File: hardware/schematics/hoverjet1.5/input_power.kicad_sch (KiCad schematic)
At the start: 12 parts, among them J1 Barrel_Jack, J2 Molex MiniFit 3.0

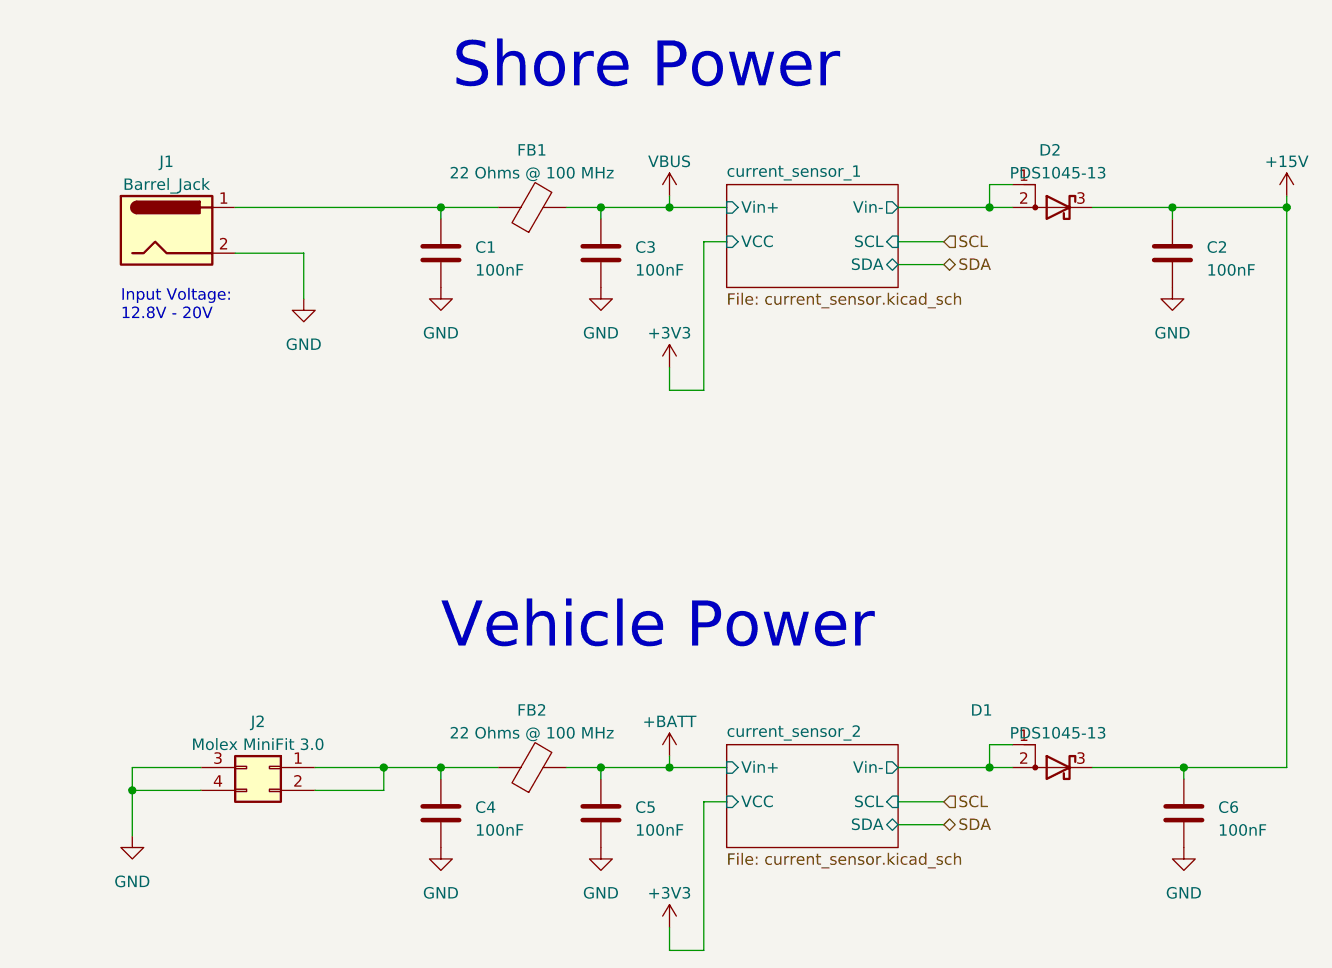
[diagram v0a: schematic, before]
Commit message: Added LM5050 ideal diode controller
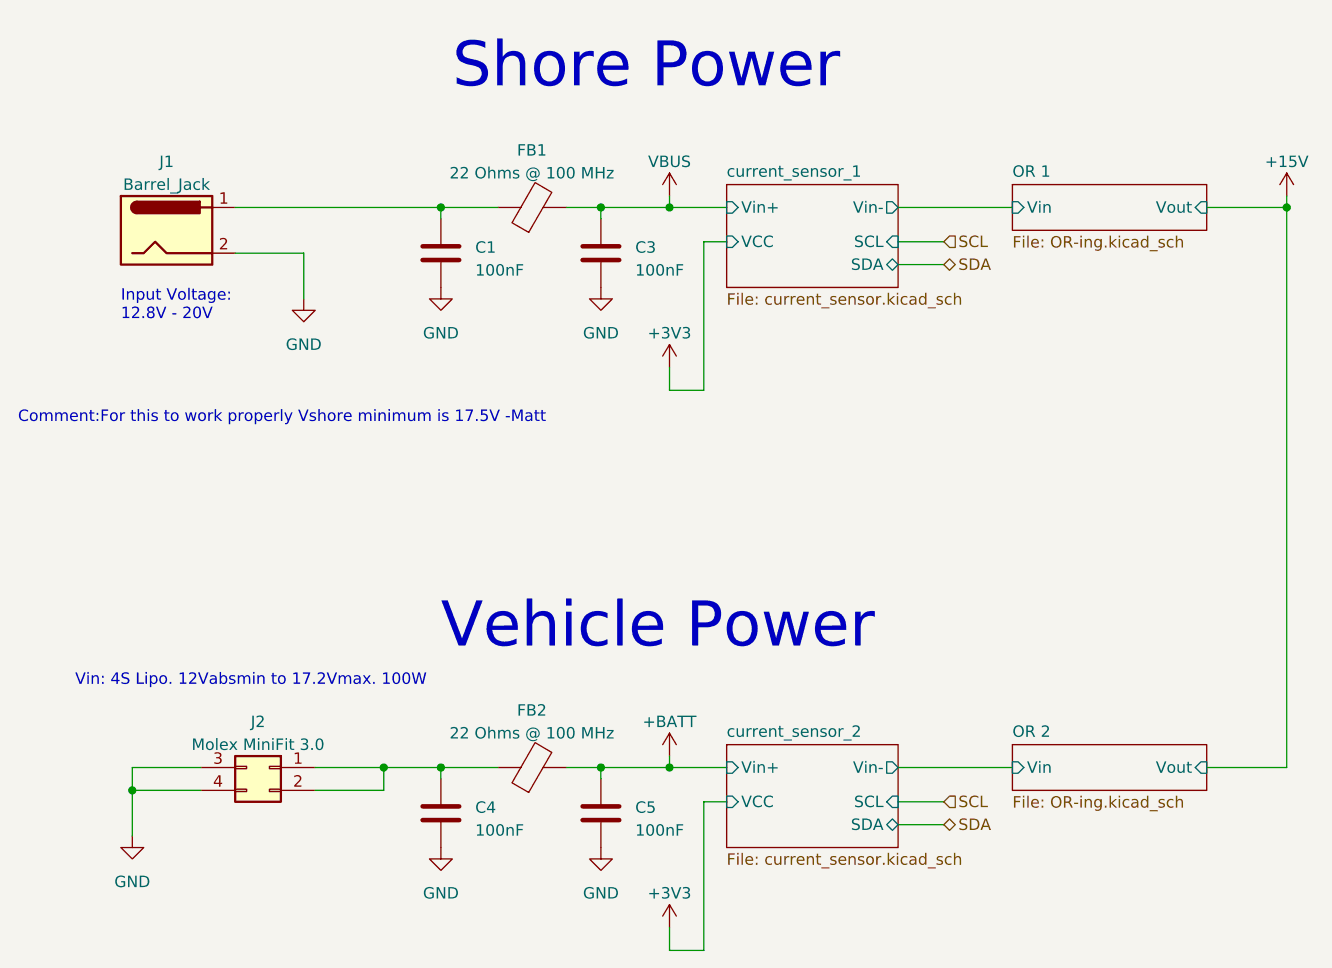
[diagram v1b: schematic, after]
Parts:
- removed C2, C6: 100nF, Capacitor_SMD:C_0201_0603Metric, symbol Device:C
- removed D1, D2: D_Schottky_AAK, Diode_SMD:D_PowerDI-5, symbol Device:D_Schottky_AAK
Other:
- added sheet OR 1 (OR-ing.kicad_sch)
- added sheet OR 2 (OR-ing.kicad_sch)
- note added: "Comment:For this to work properly Vshore minimum is 17.5V -Matt"
- note added: "Vin: 4S Lipo. 12Vabsmin to 17.2Vmax. 100W"
